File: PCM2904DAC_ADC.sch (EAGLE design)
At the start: 48 parts, among them IC1 LM358D, Q1 12MHz, X1 V+, D-, D+, GND

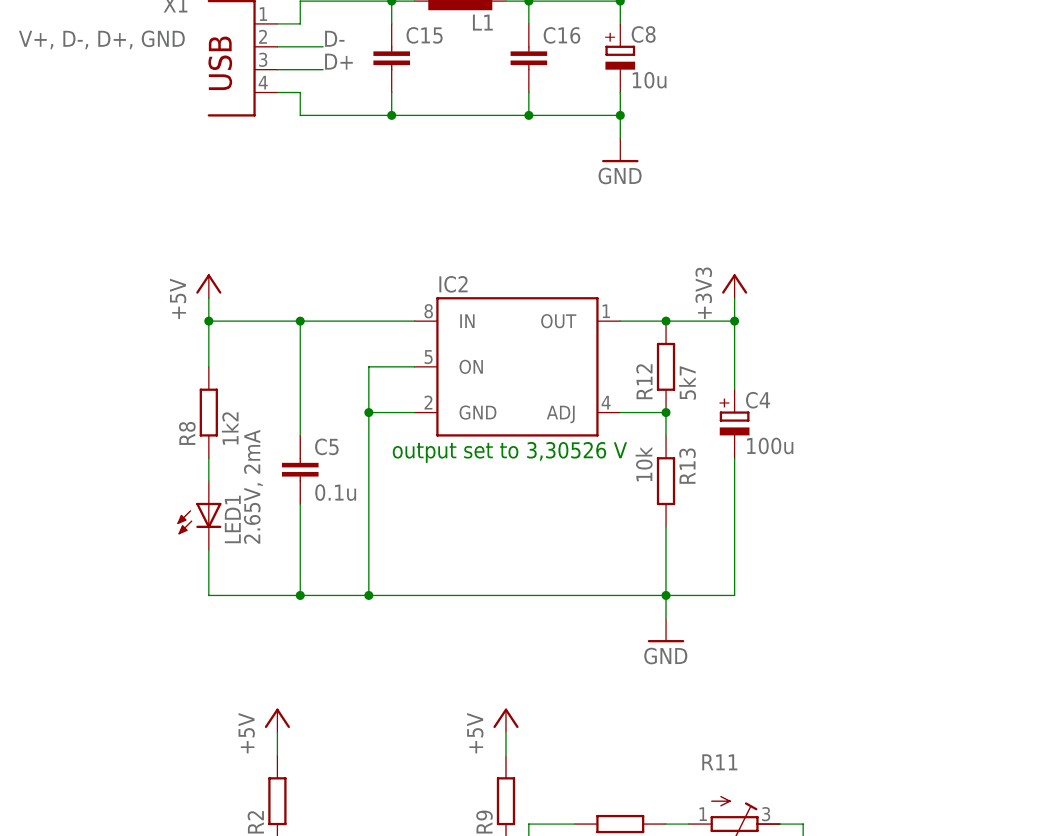
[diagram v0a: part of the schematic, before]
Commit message: agregada R de 100 ohms en el sch. FALTA ACOMODARLA  EN EL PCB
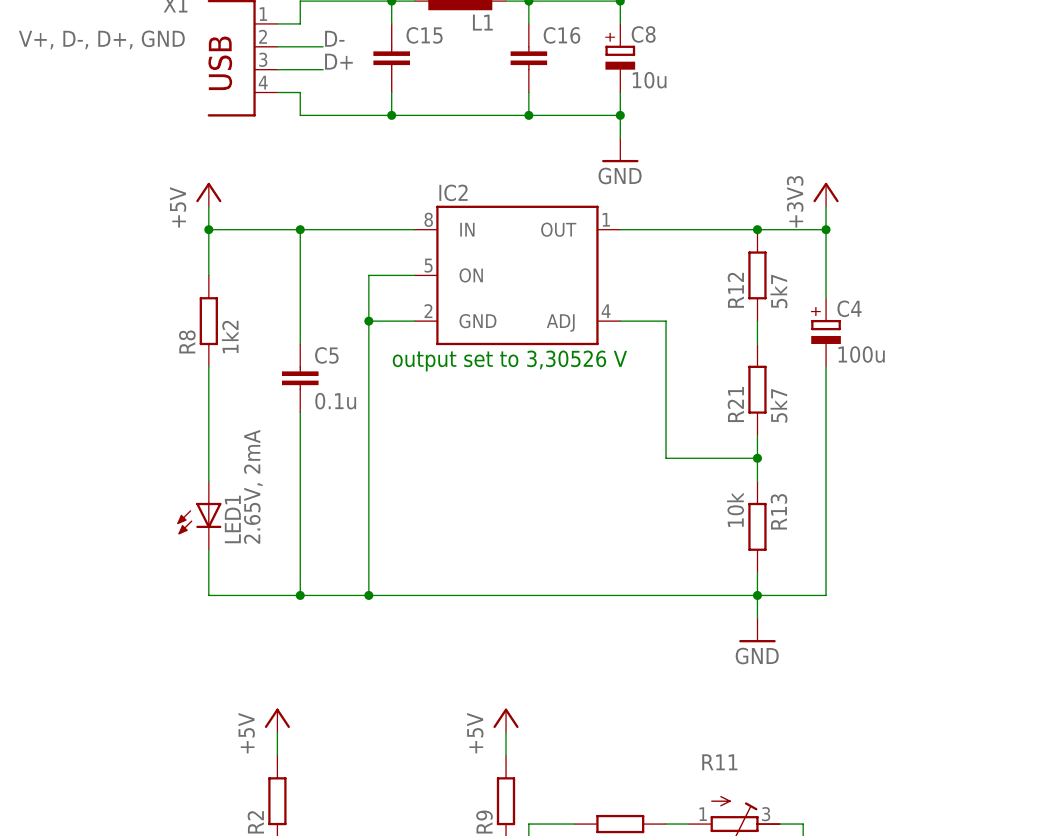
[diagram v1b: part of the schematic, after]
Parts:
- added R21: 5k7, rcl:R-EU_R1206
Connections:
- removed net N$41: IC2.ADJ, R12.1, R13.1
- new net N$23: R12.1, R21.2
- new net N$26: IC2.ADJ, R13.1, R21.1
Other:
- moved on the sheet: C4, C5, IC2, R12, R13, R8
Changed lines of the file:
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@@
 <part name="U$8" library="bleep t2" deviceset="1/8STEREO" device=""/>
 <part name="U$1" library="bleep t2" deviceset="1/8STEREO" device=""/>
+<part name="R21" library="rcl" deviceset="R-EU_" device="R1206" value="5k7"/>
 </parts>
 <sheets>
 <sheet>
 <plain>
-<text x="-66.04" y="30.48" size="1.778" layer="91">output set to 3,30526 V</text>
+<text x="-66.04" y="40.64" size="1.778" layer="91">output set to 3,30526 V</text>
 </plain>
 <instances>
@@
 <attribute name="VALUE" x="-88.9" y="76.2" size="1.778" layer="96" rot="MR0"/>
 </instance>
-<instance part="GND2" gate="1" x="-35.56" y="10.16"/>
-<instance part="C4" gate="G$1" x="-27.94" y="35.56"/>
+<instance part="GND2" gate="1" x="-25.4" y="10.16"/>
+<instance part="C4" gate="G$1" x="-17.78" y="45.72"/>
 <instance part="R4" gate="G$1" x="48.26" y="68.58"/>
 <instance part="R5" gate="G$1" x="38.1" y="66.04"/>
-<instance part="C5" gate="G$1" x="-76.2" y="30.48"/>
+<instance part="C5" gate="G$1" x="-76.2" y="40.64"/>
 <instance part="R6" gate="G$1" x="22.86" y="71.12" rot="R270"/>
 <instance part="C6" gate="G$1" x="22.86" y="58.42"/>
@@
 <instance part="C13" gate="G$1" x="116.84" y="45.72" rot="R90"/>
 <instance part="C14" gate="G$1" x="116.84" y="40.64" rot="R90"/>
-<instance part="R8" gate="G$1" x="-86.36" y="35.56" rot="R90"/>
+<instance part="R8" gate="G$1" x="-86.36" y="45.72" rot="R90"/>
 <instance part="PCM2904" gate="PCM2904" x="78.74" y="45.72"/>
 <instance part="LED1" gate="G$1" x="-86.36" y="25.4"/>
-<instance part="IC2" gate="A" x="-53.34" y="40.64"/>
-<instance part="R12" gate="G$1" x="-35.56" y="40.64" rot="R90"/>
-<instance part="R13" gate="G$1" x="-35.56" y="27.94" rot="R270"/>
+<instance part="IC2" gate="A" x="-53.34" y="50.8"/>
+<instance part="R12" gate="G$1" x="-25.4" y="50.8" rot="R90"/>
+<instance part="R13" gate="G$1" x="-25.4" y="22.86" rot="R270"/>
 <instance part="IC1" gate="A" x="-40.64" y="-22.86" rot="MR180"/>
 <instance part="R2" gate="G$1" x="-78.74" y="-7.62" rot="R90"/>
@@
 <instance part="GND5" gate="1" x="-78.74" y="-40.64"/>
 <instance part="GND6" gate="1" x="-53.34" y="-45.72"/>
-<instance part="P+4" gate="1" x="-86.36" y="50.8"/>
-<instance part="+3V1" gate="G$1" x="-27.94" y="50.8"/>
+<instance part="P+4" gate="1" x="-86.36" y="60.96"/>
+<instance part="+3V1" gate="G$1" x="-17.78" y="60.96"/>
 <instance part="GND7" gate="1" x="60.96" y="55.88"/>
 <instance part="GND8" gate="1" x="63.5" y="20.32"/>
@@
 <instance part="U$8" gate="G$1" x="-104.14" y="-25.4" rot="MR180"/>
 <instance part="U$1" gate="G$1" x="-104.14" y="-78.74" rot="MR180"/>
+<instance part="R21" gate="G$1" x="-25.4" y="38.1" rot="R90"/>
 </instances>
 <busses>
@@
 <net name="GND" class="0">
 <segment>
-<wire x1="-35.56" y1="12.7" x2="-35.56" y2="15.24" width="0.1524" layer="91"/>
-<wire x1="-27.94" y1="30.48" x2="-27.94" y2="15.24" width="0.1524" layer="91"/>
-<wire x1="-27.94" y1="15.24" x2="-35.56" y2="15.24" width="0.1524" layer="91"/>
-<wire x1="-76.2" y1="25.4" x2="-76.2" y2="15.24" width="0.1524" layer="91"/>
+<wire x1="-25.4" y1="12.7" x2="-25.4" y2="15.24" width="0.1524" layer="91"/>
+<wire x1="-17.78" y1="40.64" x2="-17.78" y2="15.24" width="0.1524" layer="91"/>
+<wire x1="-17.78" y1="15.24" x2="-25.4" y2="15.24" width="0.1524" layer="91"/>
+<wire x1="-76.2" y1="35.56" x2="-76.2" y2="15.24" width="0.1524" layer="91"/>
 <wire x1="-76.2" y1="15.24" x2="-68.58" y2="15.24" width="0.1524" layer="91"/>
-<wire x1="-68.58" y1="15.24" x2="-35.56" y2="15.24" width="0.1524" layer="91"/>
+<wire x1="-68.58" y1="15.24" x2="-25.4" y2="15.24" width="0.1524" layer="91"/>
 <wire x1="-86.36" y1="20.32" x2="-86.36" y2="15.24" width="0.1524" layer="91"/>
 <wire x1="-86.36" y1="15.24" x2="-76.2" y2="15.24" width="0.1524" layer="91"/>
-<junction x="-35.56" y="15.24"/>
+<junction x="-25.4" y="15.24"/>
 <junction x="-76.2" y="15.24"/>
 <pinref part="GND2" gate="1" pin="GND"/>
@@
 <pinref part="LED1" gate="G$1" pin="C"/>
 <pinref part="R13" gate="G$1" pin="2"/>
-<wire x1="-35.56" y1="22.86" x2="-35.56" y2="15.24" width="0.1524" layer="91"/>
+<wire x1="-25.4" y1="17.78" x2="-25.4" y2="15.24" width="0.1524" layer="91"/>
 <pinref part="IC2" gate="A" pin="GND"/>
-<wire x1="-63.5" y1="35.56" x2="-68.58" y2="35.56" width="0.1524" layer="91"/>
-<wire x1="-68.58" y1="35.56" x2="-68.58" y2="15.24" width="0.1524" layer="91"/>
+<wire x1="-63.5" y1="45.72" x2="-68.58" y2="45.72" width="0.1524" layer="91"/>
+<wire x1="-68.58" y1="45.72" x2="-68.58" y2="15.24" width="0.1524" layer="91"/>
 <junction x="-68.58" y="15.24"/>
 <pinref part="IC2" gate="A" pin="ON"/>
-<wire x1="-63.5" y1="40.64" x2="-68.58" y2="40.64" width="0.1524" layer="91"/>
-<wire x1="-68.58" y1="40.64" x2="-68.58" y2="35.56" width="0.1524" layer="91"/>
-<junction x="-68.58" y="35.56"/>
+<wire x1="-63.5" y1="50.8" x2="-68.58" y2="50.8" width="0.1524" layer="91"/>
+<wire x1="-68.58" y1="50.8" x2="-68.58" y2="45.72" width="0.1524" layer="91"/>
+<junction x="-68.58" y="45.72"/>
 </segment>
 <segment>
@@
 <net name="N$25" class="0">
 <segment>
-<wire x1="-86.36" y1="30.48" x2="-86.36" y2="27.94" width="0.1524" layer="91"/>
+<wire x1="-86.36" y1="40.64" x2="-86.36" y2="27.94" width="0.1524" layer="91"/>
 <pinref part="R8" gate="G$1" pin="1"/>
 <pinref part="LED1" gate="G$1" pin="A"/>
-</segment>
-</net>
-<net name="N$41" class="0">
-<segment>
-<pinref part="R12" gate="G$1" pin="1"/>
-<pinref part="R13" gate="G$1" pin="1"/>
-<wire x1="-35.56" y1="35.56" x2="-35.56" y2="33.02" width="0.1524" layer="91"/>
-<pinref part="IC2" gate="A" pin="ADJ"/>
-<wire x1="-40.64" y1="35.56" x2="-35.56" y2="35.56" width="0.1524" layer="91"/>
-<junction x="-35.56" y="35.56"/>
 </segment>
 </net>
@@
 </segment>
 <segment>
-<wire x1="-76.2" y1="45.72" x2="-76.2" y2="33.02" width="0.1524" layer="91"/>
-<wire x1="-86.36" y1="40.64" x2="-86.36" y2="45.72" width="0.1524" layer="91"/>
-<wire x1="-86.36" y1="45.72" x2="-76.2" y2="45.72" width="0.1524" layer="91"/>
-<junction x="-76.2" y="45.72"/>
+<wire x1="-76.2" y1="55.88" x2="-76.2" y2="43.18" width="0.1524" layer="91"/>
+<wire x1="-86.36" y1="50.8" x2="-86.36" y2="55.88" width="0.1524" layer="91"/>
+<wire x1="-86.36" y1="55.88" x2="-76.2" y2="55.88" width="0.1524" layer="91"/>
+<junction x="-76.2" y="55.88"/>
 <pinref part="C5" gate="G$1" pin="1"/>
 <pinref part="R8" gate="G$1" pin="2"/>
 <pinref part="IC2" gate="A" pin="IN"/>
-<wire x1="-63.5" y1="45.72" x2="-76.2" y2="45.72" width="0.1524" layer="91"/>
+<wire x1="-63.5" y1="55.88" x2="-76.2" y2="55.88" width="0.1524" layer="91"/>
 <pinref part="P+4" gate="1" pin="+5V"/>
-<wire x1="-86.36" y1="48.26" x2="-86.36" y2="45.72" width="0.1524" layer="91"/>
-<junction x="-86.36" y="45.72"/>
+<wire x1="-86.36" y1="58.42" x2="-86.36" y2="55.88" width="0.1524" layer="91"/>
+<junction x="-86.36" y="55.88"/>
 </segment>
 <segment>
@@
 <pinref part="IC2" gate="A" pin="OUT"/>
 <pinref part="R12" gate="G$1" pin="2"/>
-<wire x1="-40.64" y1="45.72" x2="-35.56" y2="45.72" width="0.1524" layer="91"/>
-<wire x1="-27.94" y1="45.72" x2="-27.94" y2="38.1" width="0.1524" layer="91"/>
+<wire x1="-40.64" y1="55.88" x2="-25.4" y2="55.88" width="0.1524" layer="91"/>
+<wire x1="-17.78" y1="55.88" x2="-17.78" y2="48.26" width="0.1524" layer="91"/>
 <pinref part="C4" gate="G$1" pin="+"/>
-<wire x1="-35.56" y1="45.72" x2="-27.94" y2="45.72" width="0.1524" layer="91"/>
-<junction x="-35.56" y="45.72"/>
+<wire x1="-25.4" y1="55.88" x2="-17.78" y2="55.88" width="0.1524" layer="91"/>
+<junction x="-25.4" y="55.88"/>
 <pinref part="+3V1" gate="G$1" pin="+3V3"/>
-<wire x1="-27.94" y1="48.26" x2="-27.94" y2="45.72" width="0.1524" layer="91"/>
-<junction x="-27.94" y="45.72"/>
+<wire x1="-17.78" y1="58.42" x2="-17.78" y2="55.88" width="0.1524" layer="91"/>
+<junction x="-17.78" y="55.88"/>
 </segment>
 </net>
@@
 </segment>
 </net>
+<net name="N$23" class="0">
+<segment>
+<pinref part="R12" gate="G$1" pin="1"/>
+<pinref part="R21" gate="G$1" pin="2"/>
+<wire x1="-25.4" y1="43.18" x2="-25.4" y2="45.72" width="0.1524" layer="91"/>
+</segment>
+</net>
+<net name="N$26" class="0">
+<segment>
+<pinref part="R13" gate="G$1" pin="1"/>
+<pinref part="R21" gate="G$1" pin="1"/>
+<wire x1="-25.4" y1="27.94" x2="-25.4" y2="30.48" width="0.1524" layer="91"/>
+<pinref part="IC2" gate="A" pin="ADJ"/>
+<wire x1="-25.4" y1="30.48" x2="-25.4" y2="33.02" width="0.1524" layer="91"/>
+<wire x1="-40.64" y1="45.72" x2="-35.56" y2="45.72" width="0.1524" layer="91"/>
+<wire x1="-35.56" y1="45.72" x2="-35.56" y2="30.48" width="0.1524" layer="91"/>
+<wire x1="-35.56" y1="30.48" x2="-25.4" y2="30.48" width="0.1524" layer="91"/>
+<junction x="-25.4" y="30.48"/>
+</segment>
+</net>
